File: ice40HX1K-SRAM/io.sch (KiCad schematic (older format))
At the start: 10 parts

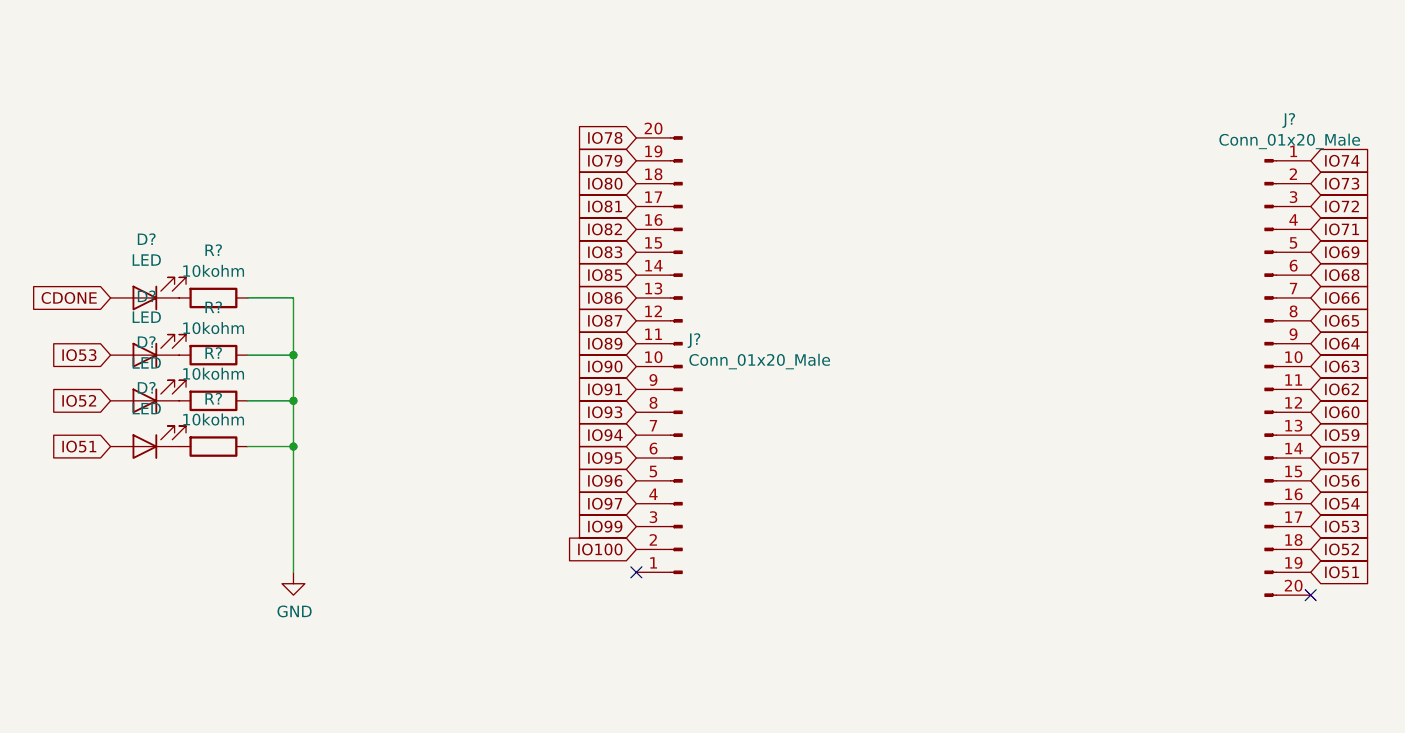
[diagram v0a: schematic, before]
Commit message: wiring FPGA nRF52 and ATSAMD11
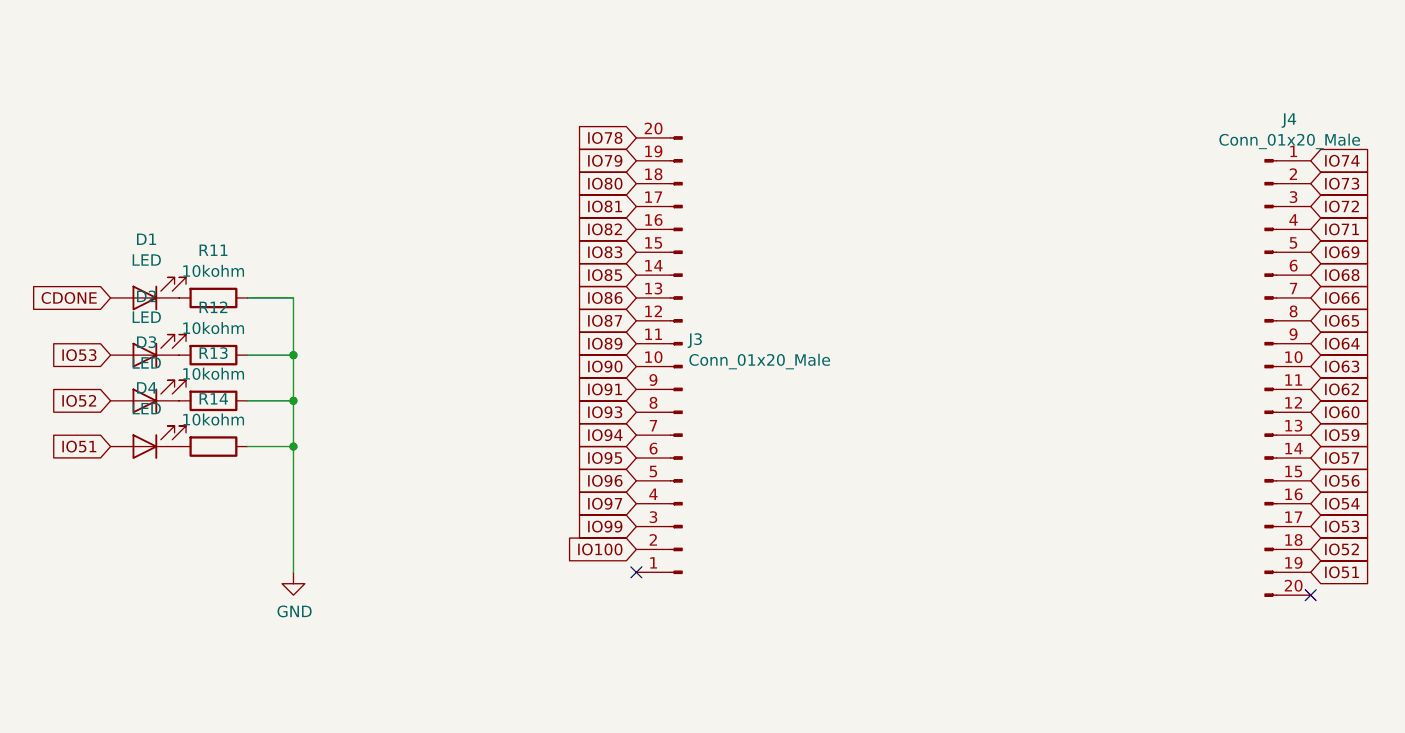
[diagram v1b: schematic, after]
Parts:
- gave numbers to parts that had none: 10
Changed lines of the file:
@@
 P 2900 3000
 AR Path="/5E677C12" Ref="D?"  Part="1"
-AR Path="/5E5F7D61/5E677C12" Ref="D?"  Part="1"
-F 0 "D?" H 2893 2745 50  0000 C CNN
+AR Path="/5E5F7D61/5E677C12" Ref="D1"  Part="1"
+F 0 "D1" H 2893 2745 50  0000 C CNN
 F 1 "LED" H 2893 2836 50  0000 C CNN
 F 2 "LED_SMD:LED_1206_3216Metric" H 2900 3000 50  0001 C CNN
@@
 P 3200 3000
 AR Path="/5E677C18" Ref="R?"  Part="1"
-AR Path="/5E5F7D61/5E677C18" Ref="R?"  Part="1"
-F 0 "R?" V 2993 3000 50  0000 C CNN
+AR Path="/5E5F7D61/5E677C18" Ref="R11"  Part="1"
+F 0 "R11" V 2993 3000 50  0000 C CNN
 F 1 "10kohm" V 3084 3000 50  0000 C CNN
 F 2 "Resistor_SMD:R_1206_3216Metric" V 3130 3000 50  0001 C CNN
@@
 P 2900 3250
 AR Path="/5E677C20" Ref="D?"  Part="1"
-AR Path="/5E5F7D61/5E677C20" Ref="D?"  Part="1"
-F 0 "D?" H 2893 2995 50  0000 C CNN
+AR Path="/5E5F7D61/5E677C20" Ref="D2"  Part="1"
+F 0 "D2" H 2893 2995 50  0000 C CNN
 F 1 "LED" H 2893 3086 50  0000 C CNN
 F 2 "LED_SMD:LED_1206_3216Metric" H 2900 3250 50  0001 C CNN
@@
 P 3200 3250
 AR Path="/5E677C26" Ref="R?"  Part="1"
-AR Path="/5E5F7D61/5E677C26" Ref="R?"  Part="1"
-F 0 "R?" V 2993 3250 50  0000 C CNN
+AR Path="/5E5F7D61/5E677C26" Ref="R12"  Part="1"
+F 0 "R12" V 2993 3250 50  0000 C CNN
 F 1 "10kohm" V 3084 3250 50  0000 C CNN
 F 2 "Resistor_SMD:R_1206_3216Metric" V 3130 3250 50  0001 C CNN
@@
 P 2900 3450
 AR Path="/5E677C2E" Ref="D?"  Part="1"
-AR Path="/5E5F7D61/5E677C2E" Ref="D?"  Part="1"
-F 0 "D?" H 2893 3195 50  0000 C CNN
+AR Path="/5E5F7D61/5E677C2E" Ref="D3"  Part="1"
+F 0 "D3" H 2893 3195 50  0000 C CNN
 F 1 "LED" H 2893 3286 50  0000 C CNN
 F 2 "LED_SMD:LED_1206_3216Metric" H 2900 3450 50  0001 C CNN
@@
 P 3200 3450
 AR Path="/5E677C34" Ref="R?"  Part="1"
-AR Path="/5E5F7D61/5E677C34" Ref="R?"  Part="1"
-F 0 "R?" V 2993 3450 50  0000 C CNN
+AR Path="/5E5F7D61/5E677C34" Ref="R13"  Part="1"
+F 0 "R13" V 2993 3450 50  0000 C CNN
 F 1 "10kohm" V 3084 3450 50  0000 C CNN
 F 2 "Resistor_SMD:R_1206_3216Metric" V 3130 3450 50  0001 C CNN
@@
 P 2900 3650
 AR Path="/5E677C3C" Ref="D?"  Part="1"
-AR Path="/5E5F7D61/5E677C3C" Ref="D?"  Part="1"
-F 0 "D?" H 2893 3395 50  0000 C CNN
+AR Path="/5E5F7D61/5E677C3C" Ref="D4"  Part="1"
+F 0 "D4" H 2893 3395 50  0000 C CNN
 F 1 "LED" H 2893 3486 50  0000 C CNN
 F 2 "LED_SMD:LED_1206_3216Metric" H 2900 3650 50  0001 C CNN
@@
 P 3200 3650
 AR Path="/5E677C42" Ref="R?"  Part="1"
-AR Path="/5E5F7D61/5E677C42" Ref="R?"  Part="1"
-F 0 "R?" V 2993 3650 50  0000 C CNN
+AR Path="/5E5F7D61/5E677C42" Ref="R14"  Part="1"
+F 0 "R14" V 2993 3650 50  0000 C CNN
 F 1 "10kohm" V 3084 3650 50  0000 C CNN
 F 2 "Resistor_SMD:R_1206_3216Metric" V 3130 3650 50  0001 C CNN
@@
 IO100
 $Comp
-L Connector:Conn_01x20_Male J?
+L Connector:Conn_01x20_Male J4
 U 1 1 5E67DAE5
 P 7800 3300
-F 0 "J?" H 7908 4381 50  0000 C CNN
+F 0 "J4" H 7908 4381 50  0000 C CNN
 F 1 "Conn_01x20_Male" H 7908 4290 50  0000 C CNN
 F 2 "Connector_PinHeader_2.54mm:PinHeader_1x20_P2.54mm_Vertical" H 7800 3300 50  0001 C CNN
@@
 $EndComp
 $Comp
-L Connector:Conn_01x20_Male J?
+L Connector:Conn_01x20_Male J3
 U 1 1 5E67DAEB
 P 5250 3300
-F 0 "J?" H 5222 3182 50  0000 R CNN
+F 0 "J3" H 5222 3182 50  0000 R CNN
 F 1 "Conn_01x20_Male" H 5222 3273 50  0000 R CNN
 F 2 "Connector_PinHeader_2.54mm:PinHeader_1x20_P2.54mm_Vertical" H 5250 3300 50  0001 C CNN
@@
 NoConn ~ 5050 4200
 $Comp
-L power:GND #PWR?
+L power:GND #PWR018
 U 1 1 5E61E4BE
 P 3550 4200
-F 0 "#PWR?" H 3550 3950 50  0001 C CNN
+F 0 "#PWR018" H 3550 3950 50  0001 C CNN
 F 1 "GND" H 3555 4027 50  0000 C CNN
 F 2 "" H 3550 4200 50  0001 C CNN

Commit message: wiring FPGA
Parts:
- removed J4: Conn_01x20_Male, Connector_PinHeader_2.54mm:PinHeader_1x20_P2.54mm_Vertical, symbol Connector:Conn_01x20_Male
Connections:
- net IO100 is gone; now on net GND: J3.2 (Pin_2)
- net +3V3: now reaches J3.1 (Pin_1)
- no-connect marks 2 -> 0
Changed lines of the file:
@@
 	3550 3650 3550 3450
 Connection ~ 3550 3450
-Text GLabel 8000 4200 2    50   Input ~ 0
-IO51
-Text GLabel 8000 4100 2    50   Input ~ 0
-IO52
-Text GLabel 8000 4000 2    50   Input ~ 0
-IO53
-Text GLabel 8000 3900 2    50   Input ~ 0
-IO54
-Text GLabel 8000 3800 2    50   Input ~ 0
-IO56
-Text GLabel 8000 3700 2    50   Input ~ 0
-IO57
-Text GLabel 8000 3600 2    50   Input ~ 0
-IO59
-Text GLabel 8000 3500 2    50   Input ~ 0
-IO60
-Text GLabel 8000 3400 2    50   Input ~ 0
-IO62
-Text GLabel 8000 3300 2    50   Input ~ 0
-IO63
-Text GLabel 8000 3200 2    50   Input ~ 0
-IO64
-Text GLabel 8000 3100 2    50   Input ~ 0
-IO65
-Text GLabel 8000 3000 2    50   Input ~ 0
-IO66
-Text GLabel 8000 2900 2    50   Input ~ 0
-IO68
-Text GLabel 8000 2800 2    50   Input ~ 0
-IO69
-Text GLabel 8000 2700 2    50   Input ~ 0
-IO71
-Text GLabel 8000 2600 2    50   Input ~ 0
-IO72
-Text GLabel 8000 2500 2    50   Input ~ 0
-IO73
-Text GLabel 8000 2400 2    50   Input ~ 0
-IO74
 Text GLabel 5050 2300 0    50   Input ~ 0
 IO78
@@
 Text GLabel 5050 4000 0    50   Input ~ 0
 IO99
-Text GLabel 5050 4100 0    50   Input ~ 0
-IO100
-$Comp
-L Connector:Conn_01x20_Male J4
-U 1 1 5E67DAE5
-P 7800 3300
-F 0 "J4" H 7908 4381 50  0000 C CNN
-F 1 "Conn_01x20_Male" H 7908 4290 50  0000 C CNN
-F 2 "Connector_PinHeader_2.54mm:PinHeader_1x20_P2.54mm_Vertical" H 7800 3300 50  0001 C CNN
-F 3 "~" H 7800 3300 50  0001 C CNN
-	1    7800 3300
-	1    0    0    -1
-$EndComp
 $Comp
 L Connector:Conn_01x20_Male J3
@@
 	-1   0    0    1
 $EndComp
-NoConn ~ 8000 4300
-NoConn ~ 5050 4200
 $Comp
 L power:GND #PWR018
@@
 	3550 3650 3550 4200
 Connection ~ 3550 3650
+$Comp
+L power:GND #PWR098
+U 1 1 5E64C279
+P 4200 4600
+F 0 "#PWR098" H 4200 4350 50  0001 C CNN
+F 1 "GND" H 4205 4427 50  0000 C CNN
+F 2 "" H 4200 4600 50  0001 C CNN
+F 3 "" H 4200 4600 50  0001 C CNN
+	1    4200 4600
+	1    0    0    -1
+$EndComp
+$Comp
+L power:+3V3 #PWR099
+U 1 1 5E64C825
+P 4250 3250
+F 0 "#PWR099" H 4250 3100 50  0001 C CNN
+F 1 "+3V3" H 4265 3423 50  0000 C CNN
+F 2 "" H 4250 3250 50  0001 C CNN
+F 3 "" H 4250 3250 50  0001 C CNN
+	1    4250 3250
+	1    0    0    -1
+$EndComp
+Wire Wire Line
+	4200 4600 4200 4100
+Wire Wire Line
+	4200 4100 5050 4100
+Wire Wire Line
+	5050 4200 4400 4200
+Wire Wire Line
+	4400 4200 4400 3600
+Wire Wire Line
+	4400 3600 4250 3600
+Wire Wire Line
+	4250 3600 4250 3250
 $EndSCHEMATC

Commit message: wiring FPGA
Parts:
- R11, R12, R13, R14: footprint Resistor_SMD:R_1206_3216Metric -> Resistor_SMD:R_0402_1005Metric
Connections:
- net IO94 is gone; now on net IO87: J3.7 (Pin_7)
- net IO95 is gone; now on net IO89: J3.6 (Pin_6)
- net IO96 is gone; now on net IO90: J3.5 (Pin_5)
- net IO97 is gone; now on net IO91: J3.4 (Pin_4)
- net IO99 is gone; now on net IO93: J3.3 (Pin_3)
- net +3V3: now also J3.20 (Pin_20), J3.8 (Pin_8)
- net GND: now also J3.15 (Pin_15), J3.19 (Pin_19), J3.9 (Pin_9)
- net IO78: now also J3.18 (Pin_18); no longer J3.20 (Pin_20)
- net IO79: now also J3.17 (Pin_17); no longer J3.19 (Pin_19)
- net IO80: now also J3.16 (Pin_16); no longer J3.18 (Pin_18)
- net IO81: now also J3.14 (Pin_14); no longer J3.17 (Pin_17)
- net IO82: now also J3.13 (Pin_13); no longer J3.16 (Pin_16)
- net IO83: now also J3.12 (Pin_12); no longer J3.15 (Pin_15)
- net IO85: now also J3.11 (Pin_11); no longer J3.14 (Pin_14)
- net IO86: now also J3.10 (Pin_10); no longer J3.13 (Pin_13)
- net IO87: no longer J3.12 (Pin_12)
- net IO89: no longer J3.11 (Pin_11)
- net IO90: no longer J3.10 (Pin_10)
- net IO91: no longer J3.9 (Pin_9)
- net IO93: no longer J3.8 (Pin_8)
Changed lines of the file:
@@
 F 0 "R11" V 2993 3000 50  0000 C CNN
 F 1 "10kohm" V 3084 3000 50  0000 C CNN
-F 2 "Resistor_SMD:R_1206_3216Metric" V 3130 3000 50  0001 C CNN
+F 2 "Resistor_SMD:R_0402_1005Metric" V 3130 3000 50  0001 C CNN
 F 3 "~" H 3200 3000 50  0001 C CNN
 	1    3200 3000
@@
 F 0 "R12" V 2993 3250 50  0000 C CNN
 F 1 "10kohm" V 3084 3250 50  0000 C CNN
-F 2 "Resistor_SMD:R_1206_3216Metric" V 3130 3250 50  0001 C CNN
+F 2 "Resistor_SMD:R_0402_1005Metric" V 3130 3250 50  0001 C CNN
 F 3 "~" H 3200 3250 50  0001 C CNN
 	1    3200 3250
@@
 F 0 "R13" V 2993 3450 50  0000 C CNN
 F 1 "10kohm" V 3084 3450 50  0000 C CNN
-F 2 "Resistor_SMD:R_1206_3216Metric" V 3130 3450 50  0001 C CNN
+F 2 "Resistor_SMD:R_0402_1005Metric" V 3130 3450 50  0001 C CNN
 F 3 "~" H 3200 3450 50  0001 C CNN
 	1    3200 3450
@@
 F 0 "R14" V 2993 3650 50  0000 C CNN
 F 1 "10kohm" V 3084 3650 50  0000 C CNN
-F 2 "Resistor_SMD:R_1206_3216Metric" V 3130 3650 50  0001 C CNN
+F 2 "Resistor_SMD:R_0402_1005Metric" V 3130 3650 50  0001 C CNN
 F 3 "~" H 3200 3650 50  0001 C CNN
 	1    3200 3650
@@
 	3550 3650 3550 3450
 Connection ~ 3550 3450
-Text GLabel 5050 2300 0    50   Input ~ 0
+Text GLabel 5050 2500 0    50   Input ~ 0
 IO78
-Text GLabel 5050 2400 0    50   Input ~ 0
+Text GLabel 5050 2600 0    50   Input ~ 0
 IO79
-Text GLabel 5050 2500 0    50   Input ~ 0
+Text GLabel 5050 2700 0    50   Input ~ 0
 IO80
-Text GLabel 5050 2600 0    50   Input ~ 0
+Text GLabel 5050 2900 0    50   Input ~ 0
 IO81
-Text GLabel 5050 2700 0    50   Input ~ 0
+Text GLabel 5050 3000 0    50   Input ~ 0
 IO82
-Text GLabel 5050 2800 0    50   Input ~ 0
+Text GLabel 5050 3100 0    50   Input ~ 0
 IO83
-Text GLabel 5050 2900 0    50   Input ~ 0
+Text GLabel 5050 3200 0    50   Input ~ 0
 IO85
-Text GLabel 5050 3000 0    50   Input ~ 0
+Text GLabel 5050 3300 0    50   Input ~ 0
 IO86
-Text GLabel 5050 3100 0    50   Input ~ 0
+Text GLabel 5050 3600 0    50   Input ~ 0
 IO87
-Text GLabel 5050 3200 0    50   Input ~ 0
+Text GLabel 5050 3700 0    50   Input ~ 0
 IO89
-Text GLabel 5050 3300 0    50   Input ~ 0
+Text GLabel 5050 3800 0    50   Input ~ 0
 IO90
-Text GLabel 5050 3400 0    50   Input ~ 0
+Text GLabel 5050 3900 0    50   Input ~ 0
 IO91
-Text GLabel 5050 3500 0    50   Input ~ 0
+Text GLabel 5050 4000 0    50   Input ~ 0
 IO93
-Text GLabel 5050 3600 0    50   Input ~ 0
-IO94
-Text GLabel 5050 3700 0    50   Input ~ 0
-IO95
-Text GLabel 5050 3800 0    50   Input ~ 0
-IO96
-Text GLabel 5050 3900 0    50   Input ~ 0
-IO97
-Text GLabel 5050 4000 0    50   Input ~ 0
-IO99
 $Comp
 L Connector:Conn_01x20_Male J3
@@
 L power:+3V3 #PWR099
 U 1 1 5E64C825
-P 4250 3250
-F 0 "#PWR099" H 4250 3100 50  0001 C CNN
-F 1 "+3V3" H 4265 3423 50  0000 C CNN
-F 2 "" H 4250 3250 50  0001 C CNN
-F 3 "" H 4250 3250 50  0001 C CNN
-	1    4250 3250
+P 4400 2000
+F 0 "#PWR099" H 4400 1850 50  0001 C CNN
+F 1 "+3V3" H 4415 2173 50  0000 C CNN
+F 2 "" H 4400 2000 50  0001 C CNN
+F 3 "" H 4400 2000 50  0001 C CNN
+	1    4400 2000
 	1    0    0    -1
 $EndComp
@@
 	5050 4200 4400 4200
 Wire Wire Line
-	4400 4200 4400 3600
-Wire Wire Line
-	4400 3600 4250 3600
-Wire Wire Line
-	4250 3600 4250 3250
+	4400 2000 4400 2300
+Wire Wire Line
+	4400 3500 5050 3500
+Connection ~ 4400 3500
+Wire Wire Line
+	4400 3500 4400 4200
+Wire Wire Line
+	4200 4100 4200 3400
+Wire Wire Line
+	4200 3400 5050 3400
+Connection ~ 4200 4100
+Wire Wire Line
+	4200 2400 5050 2400
+Wire Wire Line
+	4400 2300 5050 2300
+Connection ~ 4400 2300
+Wire Wire Line
+	4400 2300 4400 3500
+Wire Wire Line
+	4200 2800 5050 2800
+Connection ~ 4200 2800
+Wire Wire Line
+	4200 2800 4200 2400
+Wire Wire Line
+	4200 2800 4200 3400
+Connection ~ 4200 3400
 $EndSCHEMATC
